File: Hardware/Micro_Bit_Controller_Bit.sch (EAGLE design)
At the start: 51 parts, among them J1 Pokehome, J2 Pokehome, J3 Pokehome, J4 Pokehome, J5 Pokehome, J6 Pokehome, J7 Pokehome, J8 Pokehome, J9 QWIIC_RA, U2 micro:bit

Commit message: Control:bit logo to Controller:bit
Also bumped version to v21 in brd and sch, to ensure correct panel files are used.
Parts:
- removed U$4, U$5: LOGO-CONTROLBIT, SparkFun-Aesthetics:LOGO-CONTROLBIT
- added U$3, U$6: LOGO-CONTROLLER_BIT, SparkFun-Aesthetics:LOGO-CONTROLLER_BIT
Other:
- note added: "v21"
- note removed: "v20"

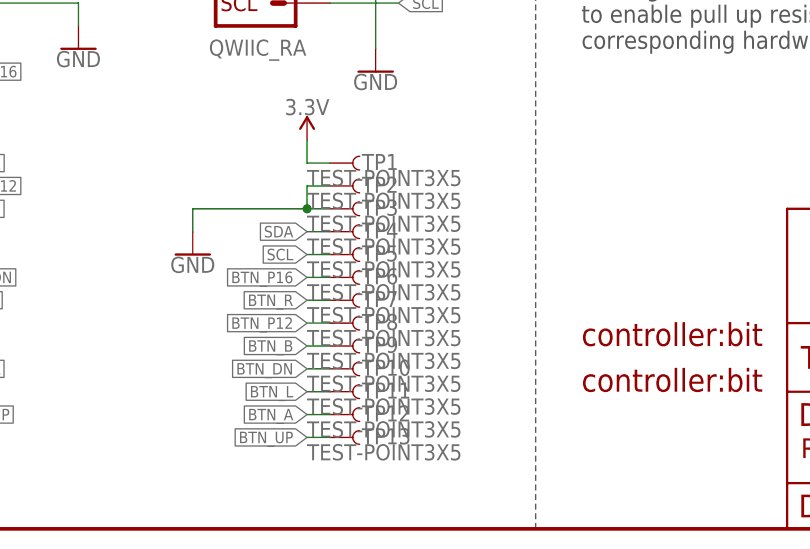
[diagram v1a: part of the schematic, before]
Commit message: Schematic cleanup
-removed pesky test point values (overlap)
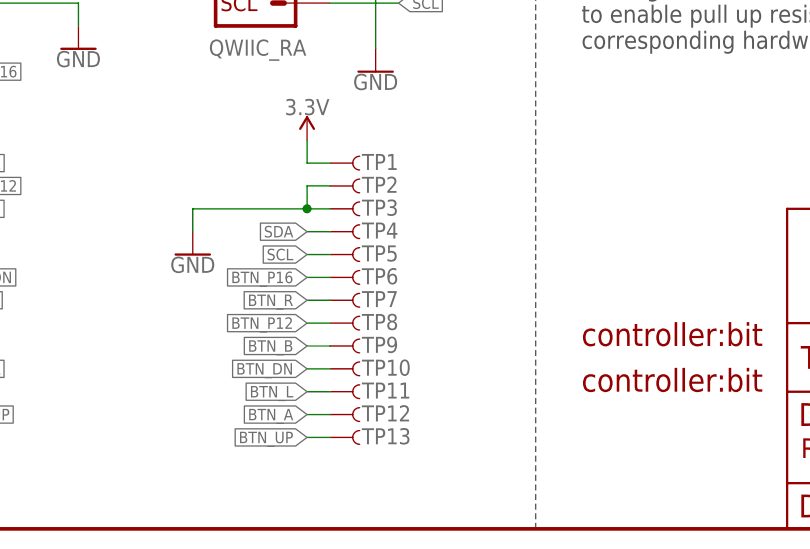
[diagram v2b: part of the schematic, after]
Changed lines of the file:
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@@
 <part name="GND10" library="SparkFun-PowerSymbols" deviceset="GND" device=""/>
 <part name="SUPPLY1" library="SparkFun-PowerSymbols" deviceset="3.3V" device=""/>
-<part name="TP1" library="SparkFun-Connectors" deviceset="TEST-POINT" device="3X5" value="TEST-POINT3X5"/>
+<part name="TP1" library="SparkFun-Connectors" deviceset="TEST-POINT" device="3X5" value=""/>
 <part name="GND11" library="SparkFun-PowerSymbols" deviceset="GND" device=""/>
 <part name="SUPPLY2" library="SparkFun-PowerSymbols" deviceset="3.3V" device=""/>
-<part name="TP2" library="SparkFun-Connectors" deviceset="TEST-POINT" device="3X5" value="TEST-POINT3X5"/>
-<part name="TP3" library="SparkFun-Connectors" deviceset="TEST-POINT" device="3X5" value="TEST-POINT3X5"/>
-<part name="TP4" library="SparkFun-Connectors" deviceset="TEST-POINT" device="3X5" value="TEST-POINT3X5"/>
-<part name="TP5" library="SparkFun-Connectors" deviceset="TEST-POINT" device="3X5" value="TEST-POINT3X5"/>
-<part name="TP6" library="SparkFun-Connectors" deviceset="TEST-POINT" device="3X5" value="TEST-POINT3X5"/>
-<part name="TP7" library="SparkFun-Connectors" deviceset="TEST-POINT" device="3X5" value="TEST-POINT3X5"/>
-<part name="TP8" library="SparkFun-Connectors" deviceset="TEST-POINT" device="3X5" value="TEST-POINT3X5"/>
-<part name="TP9" library="SparkFun-Connectors" deviceset="TEST-POINT" device="3X5" value="TEST-POINT3X5"/>
-<part name="TP10" library="SparkFun-Connectors" deviceset="TEST-POINT" device="3X5" value="TEST-POINT3X5"/>
-<part name="TP11" library="SparkFun-Connectors" deviceset="TEST-POINT" device="3X5" value="TEST-POINT3X5"/>
-<part name="TP12" library="SparkFun-Connectors" deviceset="TEST-POINT" device="3X5" value="TEST-POINT3X5"/>
-<part name="TP13" library="SparkFun-Connectors" deviceset="TEST-POINT" device="3X5" value="TEST-POINT3X5"/>
+<part name="TP2" library="SparkFun-Connectors" deviceset="TEST-POINT" device="3X5" value=""/>
+<part name="TP3" library="SparkFun-Connectors" deviceset="TEST-POINT" device="3X5" value=""/>
+<part name="TP4" library="SparkFun-Connectors" deviceset="TEST-POINT" device="3X5" value=""/>
+<part name="TP5" library="SparkFun-Connectors" deviceset="TEST-POINT" device="3X5" value=""/>
+<part name="TP6" library="SparkFun-Connectors" deviceset="TEST-POINT" device="3X5" value=""/>
+<part name="TP7" library="SparkFun-Connectors" deviceset="TEST-POINT" device="3X5" value=""/>
+<part name="TP8" library="SparkFun-Connectors" deviceset="TEST-POINT" device="3X5" value=""/>
+<part name="TP9" library="SparkFun-Connectors" deviceset="TEST-POINT" device="3X5" value=""/>
+<part name="TP10" library="SparkFun-Connectors" deviceset="TEST-POINT" device="3X5" value=""/>
+<part name="TP11" library="SparkFun-Connectors" deviceset="TEST-POINT" device="3X5" value=""/>
+<part name="TP12" library="SparkFun-Connectors" deviceset="TEST-POINT" device="3X5" value=""/>
+<part name="TP13" library="SparkFun-Connectors" deviceset="TEST-POINT" device="3X5" value=""/>
 <part name="U$3" library="SparkFun-Aesthetics" deviceset="LOGO-CONTROLLER_BIT" device=""/>
 <part name="U$6" library="SparkFun-Aesthetics" deviceset="LOGO-CONTROLLER_BIT" device=""/>
